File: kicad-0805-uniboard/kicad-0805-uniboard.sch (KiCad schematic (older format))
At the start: 145 parts, among them J1 ICSP Header, J103 BA56_3DIG_7SEG, J104 Gate Out, J105 Clock Out, J106 Clock In, J107 Pitch Out, J108 CV Out, J109 Reset In, J4 RED_STRIPE, Q1 2N7002, Q101 MMBT3906, Q102 MMBT3906, Q103 MMBT3906, Q104 MMBT3904, Q105 MMBT3904, Q2 2N7002, Q3 2N7002, Q4 2N7002, SW101 Shift, SW102 Play, SW103 Load, SW104 Save, SW105 Repeat, SW106 Mutate, SW107 Glide, SW108 SW_Push, SW109 SW_Push, SW110 SW_Push, SW111 SW_Push, SW112 SW_Push, SW113 SW_Push, SW114 SW_Push, SW115 SW_Push, SW116 Rotary_Encoder, SW117 SW_Push, SW118 SW_Push, SW119 SW_Push, SW120 SW_Push, SW121 SW_Push, SW122 SW_Push, SW123 SW_Push, SW124 SW_Push, U1 AMS1117-5.0, U101 74HC595, U102 MCP23S17, U103 74HC595, U2 AMS1117-3.3, U3 ATMega328P, U4 W25Q80DVSN, U5 TL072, U6 MCP4822, Y1 16 MHz

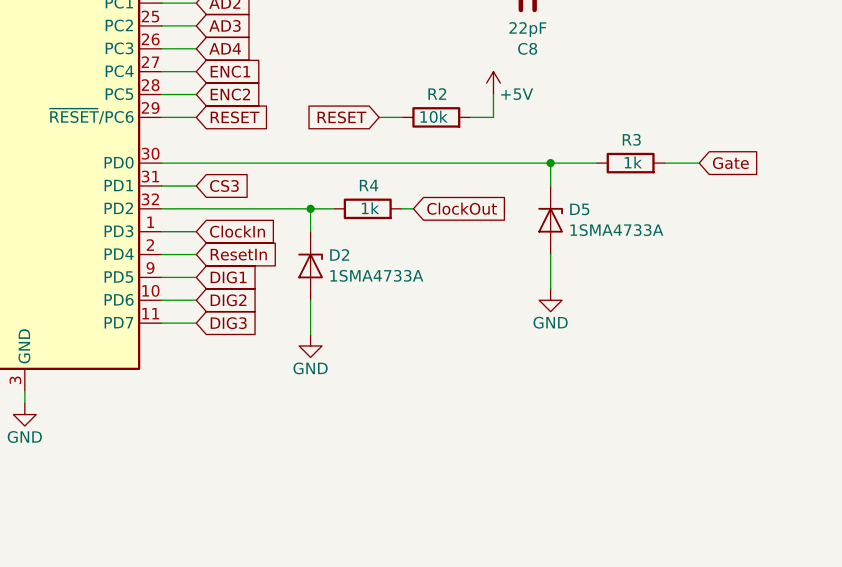
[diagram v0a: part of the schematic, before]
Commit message: Initial fp's changed. Cleared old routings.
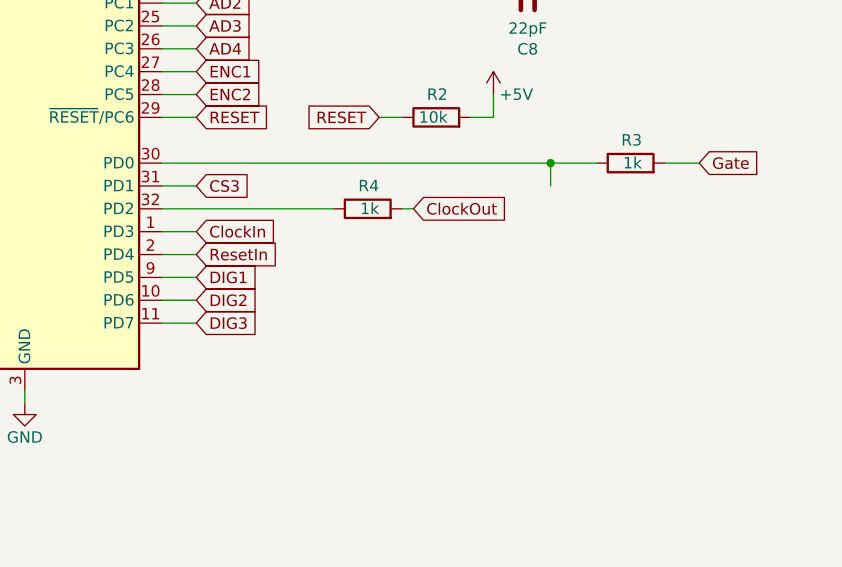
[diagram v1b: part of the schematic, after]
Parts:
- removed D2, D5: 1SMA4733A, symbol Device:D_Zener
- C10, C104, C107, C12, C2: footprint Capacitors_SMD:CP_Elec_6.3x7.7 -> Capacitor_SMD:CP_Elec_5x5.7
- C11: footprint Capacitors_SMD:CP_Elec_6.3x7.7 -> Capacitor_SMD:CP_Elec_6.3x7.7
- C16: footprint Capacitor_SMD:C_0805_2012Metric_Pad1.15x1.40mm_HandSolder -> Capacitor_SMD:CP_Elec_5x5.7
- RV101, RV102, RV103, RV104: footprint Potentiometers:Potentiometer_Alps_RK09K_Horizontal -> Eurocad:Alpha9mmPot-SemiSMD4
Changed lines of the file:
@@
 F 0 "C104" H 5315 1896 50  0000 L CNN
 F 1 "47uF" H 5315 1805 50  0000 L CNN
-F 2 "Capacitors_SMD:CP_Elec_6.3x7.7" H 5200 1850 50  0001 C CNN
+F 2 "Capacitor_SMD:CP_Elec_5x5.7" H 5200 1850 50  0001 C CNN
 F 3 "~" H 5200 1850 50  0001 C CNN
 F 4 "C108053" H 5200 1850 50  0001 C CNN "LCSC Part Number"
@@
 F 0 "C107" H 10315 4796 50  0000 L CNN
 F 1 "47uF" H 10315 4705 50  0000 L CNN
-F 2 "Capacitors_SMD:CP_Elec_6.3x7.7" H 10200 4750 50  0001 C CNN
+F 2 "Capacitor_SMD:CP_Elec_5x5.7" H 10200 4750 50  0001 C CNN
 F 3 "~" H 10200 4750 50  0001 C CNN
 F 4 "C108053" H 10200 4750 50  0001 C CNN "LCSC Part Number"
@@
 F 0 "RV102" V 11135 6150 50  0000 C CNN
 F 1 "R_POT" V 11044 6150 50  0000 C CNN
-F 2 "Potentiometers:Potentiometer_Alps_RK09K_Horizontal" H 11250 6150 50  0001 C CNN
+F 2 "Eurocad:Alpha9mmPot-SemiSMD4" H 11250 6150 50  0001 C CNN
 F 3 "~" H 11250 6150 50  0001 C CNN
 	1    11250 6150
@@
 F 0 "RV103" V 11135 6550 50  0000 C CNN
 F 1 "R_POT" V 11044 6550 50  0000 C CNN
-F 2 "Potentiometers:Potentiometer_Alps_RK09K_Horizontal" H 11250 6550 50  0001 C CNN
+F 2 "Eurocad:Alpha9mmPot-SemiSMD4" H 11250 6550 50  0001 C CNN
 F 3 "~" H 11250 6550 50  0001 C CNN
 	1    11250 6550
@@
 F 0 "RV104" V 11135 6950 50  0000 C CNN
 F 1 "R_POT" V 11044 6950 50  0000 C CNN
-F 2 "Potentiometers:Potentiometer_Alps_RK09K_Horizontal" H 11250 6950 50  0001 C CNN
+F 2 "Eurocad:Alpha9mmPot-SemiSMD4" H 11250 6950 50  0001 C CNN
 F 3 "~" H 11250 6950 50  0001 C CNN
 	1    11250 6950
@@
 F 0 "RV101" V 11135 5750 50  0000 C CNN
 F 1 "R_POT" V 11044 5750 50  0000 C CNN
-F 2 "Potentiometers:Potentiometer_Alps_RK09K_Horizontal" H 11250 5750 50  0001 C CNN
+F 2 "Eurocad:Alpha9mmPot-SemiSMD4" H 11250 5750 50  0001 C CNN
 F 3 "~" H 11250 5750 50  0001 C CNN
 	1    11250 5750
@@
 F 0 "C11" H 20700 13500 50  0000 L CNN
 F 1 "100uF" H 20700 13300 50  0000 L CNN
-F 2 "Capacitors_SMD:CP_Elec_6.3x7.7" H 20688 13250 50  0001 C CNN
+F 2 "Capacitor_SMD:CP_Elec_6.3x7.7" H 20688 13250 50  0001 C CNN
 F 3 "~" H 20650 13400 50  0001 C CNN
 	1    20650 13400
@@
 F 0 "C12" H 20400 13950 50  0000 L CNN
 F 1 "22uF" H 20350 13750 50  0000 L CNN
-F 2 "Capacitors_SMD:CP_Elec_6.3x7.7" H 20388 13700 50  0001 C CNN
+F 2 "Capacitor_SMD:CP_Elec_5x5.7" H 20388 13700 50  0001 C CNN
 F 3 "~" H 20350 13850 50  0001 C CNN
 	1    20350 13850
@@
 F 0 "C2" H 15900 13600 50  0000 L CNN
 F 1 "22uF" H 15850 13400 50  0000 L CNN
-F 2 "Capacitors_SMD:CP_Elec_6.3x7.7" H 15888 13350 50  0001 C CNN
+F 2 "Capacitor_SMD:CP_Elec_5x5.7" H 15888 13350 50  0001 C CNN
 F 3 "~" H 15850 13500 50  0001 C CNN
 	1    15850 13500
@@
 F 0 "C10" H 17750 13650 50  0000 L CNN
 F 1 "10uF" H 17750 13450 50  0000 L CNN
-F 2 "Capacitors_SMD:CP_Elec_6.3x7.7" H 17738 13400 50  0001 C CNN
+F 2 "Capacitor_SMD:CP_Elec_5x5.7" H 17738 13400 50  0001 C CNN
 F 3 "~" H 17700 13550 50  0001 C CNN
 	1    17700 13550
@@
 	17750 1950 17750 2000
 $Comp
-L Device:D_Zener D5
-U 1 1 608C6B56
-P 20050 4250
-F 0 "D5" V 20004 4329 50  0000 L CNN
-F 1 "1SMA4733A" V 20095 4329 50  0000 L CNN
-F 2 "" H 20050 4250 50  0001 C CNN
-F 3 "~" H 20050 4250 50  0001 C CNN
-	1    20050 4250
-	0    1    1    0
-$EndComp
-$Comp
-L Device:D_Zener D2
-U 1 1 608C7EC8
-P 19000 4450
-F 0 "D2" V 18954 4529 50  0000 L CNN
-F 1 "1SMA4733A" V 19045 4529 50  0000 L CNN
-F 2 "" H 19000 4450 50  0001 C CNN
-F 3 "~" H 19000 4450 50  0001 C CNN
-	1    19000 4450
-	0    1    1    0
-$EndComp
-$Comp
 L Device:R R3
 U 1 1 60A0DC3F
@@
 	0    -1   -1   0
 $EndComp
-$Comp
-L power:GND #PWR018
-U 1 1 60B54030
-P 19000 4750
-F 0 "#PWR018" H 19000 4500 50  0001 C CNN
-F 1 "GND" H 19000 4600 50  0000 C CNN
-F 2 "" H 19000 4750 50  0001 C CNN
-F 3 "" H 19000 4750 50  0001 C CNN
-	1    19000 4750
-	1    0    0    -1
-$EndComp
-$Comp
-L power:GND #PWR023
-U 1 1 60B95510
-P 20050 4550
-F 0 "#PWR023" H 20050 4300 50  0001 C CNN
-F 1 "GND" H 20050 4400 50  0000 C CNN
-F 2 "" H 20050 4550 50  0001 C CNN
-F 3 "" H 20050 4550 50  0001 C CNN
-	1    20050 4550
-	1    0    0    -1
-$EndComp
-Wire Wire Line
-	18350 4200 19000 4200
-Wire Wire Line
-	19000 4300 19000 4200
-Connection ~ 19000 4200
-Wire Wire Line
-	19000 4200 19100 4200
-Wire Wire Line
-	19000 4600 19000 4750
 Wire Wire Line
 	19400 4200 19450 4200
@@
 	20050 4000 20250 4000
 Wire Wire Line
-	20050 4400 20050 4550
-Wire Wire Line
 	18350 4000 20050 4000
 Connection ~ 20050 4000
@@
 F 0 "C16" H 19300 7800 50  0000 C CNN
 F 1 "22pF" H 19300 7600 50  0000 C CNN
-F 2 "Capacitor_SMD:C_0805_2012Metric_Pad1.15x1.40mm_HandSolder" H 19488 7550 50  0001 C CNN
+F 2 "Capacitor_SMD:CP_Elec_5x5.7" H 19488 7550 50  0001 C CNN
 F 3 "~" H 19450 7700 50  0001 C CNN
 	1    19450 7700
@@
 Wire Wire Line
 	19400 2950 19300 2950
+Wire Wire Line
+	18350 4200 19100 4200
 Wire Bus Line
 	3750 1650 3750 2350

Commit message: Forgot some schematic stuff. More placement.
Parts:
- added C5, C6: 100nF, Capacitor_SMD:C_0805_2012Metric_Pad1.15x1.40mm_HandSolder, symbol Device:C
- C101: footprint Capacitors_SMD:CP_Elec_6.3x7.7 -> Capacitor_SMD:CP_Elec_6.3x7.7
- C16: footprint Capacitor_SMD:CP_Elec_5x5.7 -> Capacitor_SMD:C_0805_2012Metric_Pad1.15x1.40mm_HandSolder
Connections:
- net +12V: now also C11.1, L2.1; no longer D3.1 (K), L2.2
- net +5V: now also U3.18 (AVCC), U3.20 (AREF), C5.2, C6.2
- net -12V: now also C12.2, L3.1; no longer D4.2 (A), L3.2
- net GND: now also C5.1, C6.1
- new net: D3.1 (K), L2.2
- new net: D4.2 (A), L3.2
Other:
- moved on the sheet: L2, L3
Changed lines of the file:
@@
 F 0 "C101" H 9915 1696 50  0000 L CNN
 F 1 "10uF" H 9915 1605 50  0000 L CNN
-F 2 "Capacitors_SMD:CP_Elec_6.3x7.7" H 9800 1650 50  0001 C CNN
+F 2 "Capacitor_SMD:CP_Elec_6.3x7.7" H 9800 1650 50  0001 C CNN
 F 3 "~" H 9800 1650 50  0001 C CNN
 F 4 "C108053" H 9800 1650 50  0001 C CNN "LCSC Part Number"
@@
 L Device:L L2
 U 1 1 5F8531EE
-P 20050 13200
-F 0 "L2" V 20000 13200 50  0000 C CNN
-F 1 "220uH" V 20150 13200 50  0000 C CNN
-F 2 "Inductor_SMD:L_1210_3225Metric_Pad1.42x2.65mm_HandSolder" H 20050 13200 50  0001 C CNN
-F 3 "~" H 20050 13200 50  0001 C CNN
-	1    20050 13200
+P 19900 13200
+F 0 "L2" V 19850 13200 50  0000 C CNN
+F 1 "220uH" V 20000 13200 50  0000 C CNN
+F 2 "Inductor_SMD:L_1210_3225Metric_Pad1.42x2.65mm_HandSolder" H 19900 13200 50  0001 C CNN
+F 3 "~" H 19900 13200 50  0001 C CNN
+	1    19900 13200
 	0    1    1    0
 $EndComp
@@
 L Device:L L3
 U 1 1 5F8543A8
-P 20050 13600
-F 0 "L3" V 20000 13600 50  0000 C CNN
-F 1 "220uH" V 20150 13600 50  0000 C CNN
-F 2 "Inductor_SMD:L_1210_3225Metric_Pad1.42x2.65mm_HandSolder" H 20050 13600 50  0001 C CNN
-F 3 "~" H 20050 13600 50  0001 C CNN
-	1    20050 13600
+P 19900 13600
+F 0 "L3" V 19850 13600 50  0000 C CNN
+F 1 "220uH" V 20000 13600 50  0000 C CNN
+F 2 "Inductor_SMD:L_1210_3225Metric_Pad1.42x2.65mm_HandSolder" H 19900 13600 50  0001 C CNN
+F 3 "~" H 19900 13600 50  0001 C CNN
+	1    19900 13600
 	0    1    1    0
 $EndComp
@@
 L power:+12V #PWR0131
 U 1 1 5FA2B044
-P 19800 12950
-F 0 "#PWR0131" H 19800 12800 50  0001 C CNN
-F 1 "+12V" H 19815 13123 50  0000 C CNN
-F 2 "" H 19800 12950 50  0001 C CNN
-F 3 "" H 19800 12950 50  0001 C CNN
-	1    19800 12950
+P 20150 12950
+F 0 "#PWR0131" H 20150 12800 50  0001 C CNN
+F 1 "+12V" H 20165 13123 50  0000 C CNN
+F 2 "" H 20150 12950 50  0001 C CNN
+F 3 "" H 20150 12950 50  0001 C CNN
+	1    20150 12950
 	1    0    0    -1
 $EndComp
@@
 L power:-12V #PWR0132
 U 1 1 5FA2C598
-P 19800 13900
-F 0 "#PWR0132" H 19800 14000 50  0001 C CNN
-F 1 "-12V" H 19815 14073 50  0000 C CNN
-F 2 "" H 19800 13900 50  0001 C CNN
-F 3 "" H 19800 13900 50  0001 C CNN
-	1    19800 13900
+P 20100 13900
+F 0 "#PWR0132" H 20100 14000 50  0001 C CNN
+F 1 "-12V" H 20115 14073 50  0000 C CNN
+F 2 "" H 20100 13900 50  0001 C CNN
+F 3 "" H 20100 13900 50  0001 C CNN
+	1    20100 13900
 	1    0    0    1
 $EndComp
 Wire Wire Line
-	19700 13200 19800 13200
+	20150 12950 20150 13000
 Wire Wire Line
-	19800 12950 19800 13000
-Connection ~ 19800 13200
-Wire Wire Line
-	19800 13200 19900 13200
-Wire Wire Line
-	19700 13600 19800 13600
-Wire Wire Line
-	19800 13600 19800 13850
-Connection ~ 19800 13600
-Wire Wire Line
-	19800 13600 19900 13600
-Wire Wire Line
-	20200 13600 20350 13600
+	20050 13600 20100 13600
 Wire Wire Line
 	20350 13600 20350 13700
 Wire Wire Line
-	20200 13200 20650 13200
+	20050 13200 20150 13200
 Wire Wire Line
 	20650 13200 20650 13250
@@
 L power:PWR_FLAG #FLG0104
 U 1 1 5FC138A9
-P 20100 12800
-F 0 "#FLG0104" H 20100 12875 50  0001 C CNN
-F 1 "PWR_FLAG" H 20100 12974 50  0000 C CNN
-F 2 "" H 20100 12800 50  0001 C CNN
-F 3 "~" H 20100 12800 50  0001 C CNN
-	1    20100 12800
+P 20450 12800
+F 0 "#FLG0104" H 20450 12875 50  0001 C CNN
+F 1 "PWR_FLAG" H 20450 12974 50  0000 C CNN
+F 2 "" H 20450 12800 50  0001 C CNN
+F 3 "~" H 20450 12800 50  0001 C CNN
+	1    20450 12800
 	1    0    0    -1
 $EndComp
-$Comp
-L power:PWR_FLAG #FLG0105
-U 1 1 5FD56C8E
-P 19500 14050
-F 0 "#FLG0105" H 19500 14125 50  0001 C CNN
-F 1 "PWR_FLAG" H 19500 14224 50  0000 C CNN
-F 2 "" H 19500 14050 50  0001 C CNN
-F 3 "~" H 19500 14050 50  0001 C CNN
-	1    19500 14050
-	1    0    0    1
-$EndComp
-Wire Wire Line
-	19800 13850 19500 13850
-Wire Wire Line
-	19500 13850 19500 14050
-Connection ~ 19800 13850
-Wire Wire Line
-	19800 13850 19800 13900
 Wire Wire Line
-	20100 12800 20100 13000
+	20450 12800 20450 13000
 Wire Wire Line
-	20100 13000 19800 13000
-Connection ~ 19800 13000
+	20450 13000 20150 13000
+Connection ~ 20150 13000
 Wire Wire Line
-	19800 13000 19800 13200
+	20150 13000 20150 13200
 $Comp
 L Device:CP C2
@@
 L power:+5V #PWR012
 U 1 1 607C1AFC
-P 17650 1900
-F 0 "#PWR012" H 17650 1750 50  0001 C CNN
-F 1 "+5V" H 17650 2040 50  0000 C CNN
-F 2 "" H 17650 1900 50  0001 C CNN
-F 3 "" H 17650 1900 50  0001 C CNN
-	1    17650 1900
+P 17650 1750
+F 0 "#PWR012" H 17650 1600 50  0001 C CNN
+F 1 "+5V" H 17650 1890 50  0000 C CNN
+F 2 "" H 17650 1750 50  0001 C CNN
+F 3 "" H 17650 1750 50  0001 C CNN
+	1    17650 1750
 	1    0    0    -1
 $EndComp
 Wire Wire Line
-	17750 1950 17650 1950
-Wire Wire Line
-	17650 1950 17650 1900
-Wire Wire Line
-	17750 1950 17750 2000
+	17650 1800 17650 1750
 $Comp
 L Device:R R3
@@
 F 0 "C16" H 19300 7800 50  0000 C CNN
 F 1 "22pF" H 19300 7600 50  0000 C CNN
-F 2 "Capacitor_SMD:CP_Elec_5x5.7" H 19488 7550 50  0001 C CNN
+F 2 "Capacitor_SMD:C_0805_2012Metric_Pad1.15x1.40mm_HandSolder" H 19488 7550 50  0001 C CNN
 F 3 "~" H 19450 7700 50  0001 C CNN
 	1    19450 7700
@@
 Wire Wire Line
 	18350 4200 19100 4200
+Wire Wire Line
+	19700 13600 19750 13600
+Wire Wire Line
+	19700 13200 19750 13200
+Connection ~ 20100 13850
+Wire Wire Line
+	20100 13850 20100 13900
+Wire Wire Line
+	20100 13600 20100 13850
+Wire Wire Line
+	19800 13850 19800 14050
+Wire Wire Line
+	20100 13850 19800 13850
+$Comp
+L power:PWR_FLAG #FLG0105
+U 1 1 5FD56C8E
+P 19800 14050
+F 0 "#FLG0105" H 19800 14125 50  0001 C CNN
+F 1 "PWR_FLAG" H 19800 14224 50  0000 C CNN
+F 2 "" H 19800 14050 50  0001 C CNN
+F 3 "~" H 19800 14050 50  0001 C CNN
+	1    19800 14050
+	1    0    0    1
+$EndComp
+Connection ~ 20150 13200
+Wire Wire Line
+	20150 13200 20650 13200
+Connection ~ 20100 13600
+Wire Wire Line
+	20100 13600 20350 13600
+$Comp
+L Device:C C5
+U 1 1 5F42D121
+P 18200 1800
+F 0 "C5" V 17948 1800 50  0000 C CNN
+F 1 "100nF" V 18039 1800 50  0000 C CNN
+F 2 "Capacitor_SMD:C_0805_2012Metric_Pad1.15x1.40mm_HandSolder" H 18238 1650 50  0001 C CNN
+F 3 "~" H 18200 1800 50  0001 C CNN
+	1    18200 1800
+	0    1    1    0
+$EndComp
+$Comp
+L power:GND #PWR?
+U 1 1 5F53A6C0
+P 18450 1900
+F 0 "#PWR?" H 18450 1650 50  0001 C CNN
+F 1 "GND" H 18600 1850 50  0000 C CNN
+F 2 "" H 18450 1900 50  0001 C CNN
+F 3 "" H 18450 1900 50  0001 C CNN
+	1    18450 1900
+	1    0    0    -1
+$EndComp
+Wire Wire Line
+	18450 1800 18450 1900
+Wire Wire Line
+	18450 1800 18350 1800
+Wire Wire Line
+	18050 1800 17850 1800
+$Comp
+L Device:C C6
+U 1 1 5F6F97E3
+P 16700 2300
+F 0 "C6" V 16448 2300 50  0000 C CNN
+F 1 "100nF" V 16539 2300 50  0000 C CNN
+F 2 "Capacitor_SMD:C_0805_2012Metric_Pad1.15x1.40mm_HandSolder" H 16738 2150 50  0001 C CNN
+F 3 "~" H 16700 2300 50  0001 C CNN
+	1    16700 2300
+	0    -1   1    0
+$EndComp
+Wire Wire Line
+	16450 2300 16550 2300
+$Comp
+L power:GND #PWR?
+U 1 1 5F758F54
+P 16450 2500
+F 0 "#PWR?" H 16450 2250 50  0001 C CNN
+F 1 "GND" H 16450 2350 50  0000 C CNN
+F 2 "" H 16450 2500 50  0001 C CNN
+F 3 "" H 16450 2500 50  0001 C CNN
+	1    16450 2500
+	1    0    0    -1
+$EndComp
+Wire Wire Line
+	16450 2300 16450 2500
+Wire Wire Line
+	16850 2300 17000 2300
+$Comp
+L power:+5V #PWR?
+U 1 1 5F80CF2E
+P 17000 2250
+F 0 "#PWR?" H 17000 2100 50  0001 C CNN
+F 1 "+5V" H 17000 2390 50  0000 C CNN
+F 2 "" H 17000 2250 50  0001 C CNN
+F 3 "" H 17000 2250 50  0001 C CNN
+	1    17000 2250
+	1    0    0    -1
+$EndComp
+Wire Wire Line
+	17000 2300 17000 2250
+Connection ~ 17000 2300
+Wire Wire Line
+	17000 2300 17150 2300
+Wire Wire Line
+	17750 1800 17650 1800
+Wire Wire Line
+	17750 1800 17850 1800
+Connection ~ 17750 1800
+Wire Wire Line
+	17750 1800 17750 2000
+Connection ~ 17850 1800
+Wire Wire Line
+	17850 1800 17850 2000
 Wire Bus Line
 	3750 1650 3750 2350

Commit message: It won't work this way!
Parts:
- removed Y1: 16 MHz, Crystal:Crystal_SMD_3225-4Pin_3.2x2.5mm_HandSoldering, symbol Device:Crystal_GND24
- added Y1: 16MHz, Crystal:Crystal_HC49-4H_Vertical, symbol Device:Crystal
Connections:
- net at C7.2, U3.7 (XTAL1/PB6): now also Y1.2
- net at C8.1, U3.8 (XTAL2/PB7): now also Y1.1
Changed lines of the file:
@@
 	20850 7550 20850 7600
 Connection ~ 20850 7550
-$Comp
-L Device:Crystal_GND24 Y1
-U 1 1 64097572
-P 19600 2950
-F 0 "Y1" V 19750 3050 50  0000 L CNN
-F 1 "16 MHz" V 19750 2600 50  0000 L CNN
-F 2 "Crystal:Crystal_SMD_3225-4Pin_3.2x2.5mm_HandSoldering" H 19600 2950 50  0001 C CNN
-F 3 "~" H 19600 2950 50  0001 C CNN
-	1    19600 2950
-	0    -1   -1   0
-$EndComp
 Connection ~ 19600 2650
 Wire Wire Line
@@
 Wire Wire Line
 	19000 3250 19600 3250
-$Comp
-L power:GND #PWR0139
-U 1 1 642FB763
-P 19900 3000
-F 0 "#PWR0139" H 19900 2750 50  0001 C CNN
-F 1 "GND" H 20000 3000 50  0000 C CNN
-F 2 "" H 19900 3000 50  0001 C CNN
-F 3 "" H 19900 3000 50  0001 C CNN
-	1    19900 3000
-	1    0    0    -1
-$EndComp
-Wire Wire Line
-	19900 2950 19900 3000
-Wire Wire Line
-	19800 2950 19900 2950
-$Comp
-L power:GND #PWR0140
-U 1 1 64352B3B
-P 19300 3000
-F 0 "#PWR0140" H 19300 2750 50  0001 C CNN
-F 1 "GND" H 19400 3000 50  0000 C CNN
-F 2 "" H 19300 3000 50  0001 C CNN
-F 3 "" H 19300 3000 50  0001 C CNN
-	1    19300 3000
-	-1   0    0    -1
-$EndComp
-Wire Wire Line
-	19300 2950 19300 3000
-Wire Wire Line
-	19400 2950 19300 2950
 Wire Wire Line
 	18350 4200 19100 4200
@@
 $EndComp
 $Comp
-L power:GND #PWR?
+L power:GND #PWR0141
 U 1 1 5F53A6C0
 P 18450 1900
-F 0 "#PWR?" H 18450 1650 50  0001 C CNN
+F 0 "#PWR0141" H 18450 1650 50  0001 C CNN
 F 1 "GND" H 18600 1850 50  0000 C CNN
 F 2 "" H 18450 1900 50  0001 C CNN
@@
 	16450 2300 16550 2300
 $Comp
-L power:GND #PWR?
+L power:GND #PWR0142
 U 1 1 5F758F54
 P 16450 2500
-F 0 "#PWR?" H 16450 2250 50  0001 C CNN
+F 0 "#PWR0142" H 16450 2250 50  0001 C CNN
 F 1 "GND" H 16450 2350 50  0000 C CNN
 F 2 "" H 16450 2500 50  0001 C CNN
@@
 	16850 2300 17000 2300
 $Comp
-L power:+5V #PWR?
+L power:+5V #PWR0143
 U 1 1 5F80CF2E
 P 17000 2250
-F 0 "#PWR?" H 17000 2100 50  0001 C CNN
+F 0 "#PWR0143" H 17000 2100 50  0001 C CNN
 F 1 "+5V" H 17000 2390 50  0000 C CNN
 F 2 "" H 17000 2250 50  0001 C CNN
@@
 Wire Wire Line
 	17850 1800 17850 2000
+$Comp
+L Device:Crystal Y1
+U 1 1 5F040CDA
+P 19600 2950
+F 0 "Y1" V 19700 3100 50  0000 C CNN
+F 1 "16MHz" V 19450 3150 50  0000 C CNN
+F 2 "Crystal:Crystal_HC49-4H_Vertical" H 19600 2950 50  0001 C CNN
+F 3 "~" H 19600 2950 50  0001 C CNN
+	1    19600 2950
+	0    -1   -1   0
+$EndComp
 Wire Bus Line
 	3750 1650 3750 2350
